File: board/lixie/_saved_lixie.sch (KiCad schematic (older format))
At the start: 41 parts, among them P1 USB_OTG, P2 CONN_01X04, SW1 SW_Push, U1 IS31FL3738, U2 MIC550x, U3 MAX40200, U4 STM32L073xZ

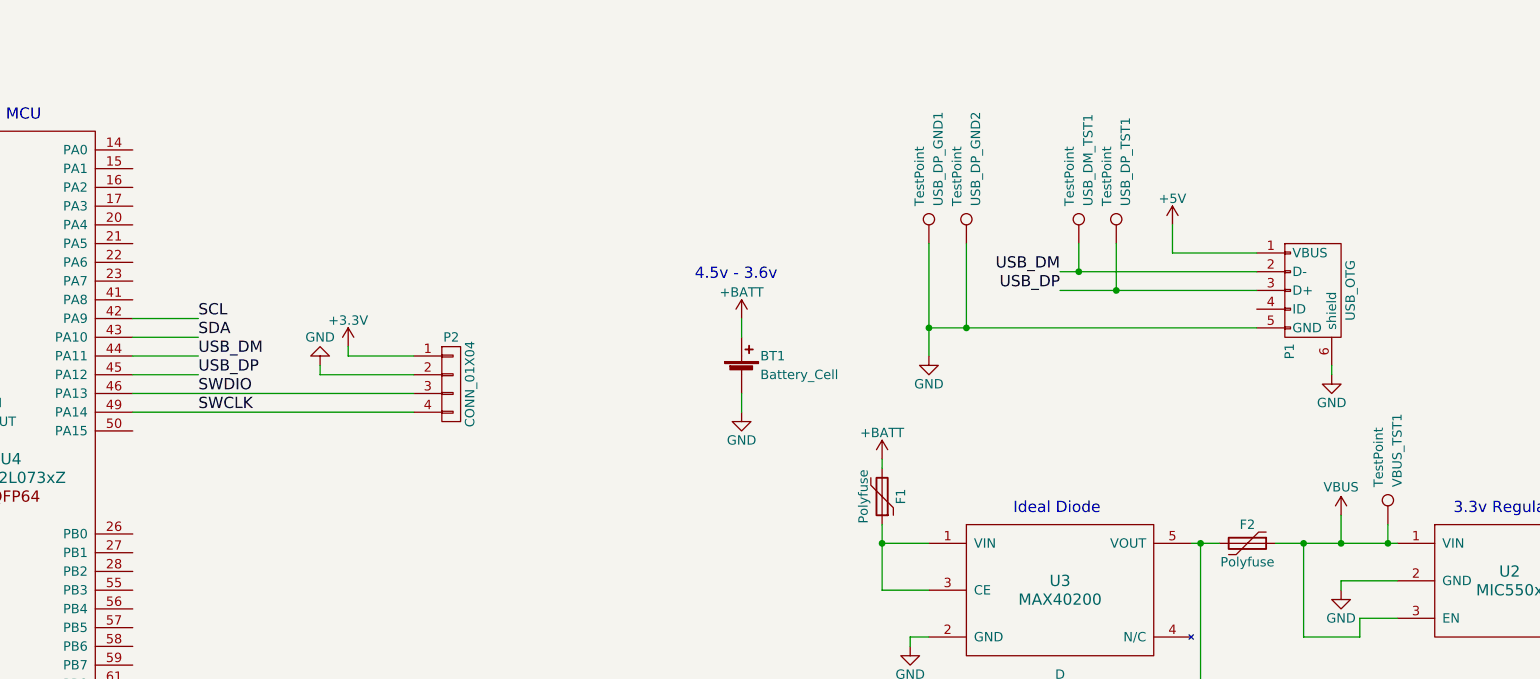
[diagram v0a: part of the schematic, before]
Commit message: apparently I routed EVERY FUCKING LED WRONG so now I gotta fix it
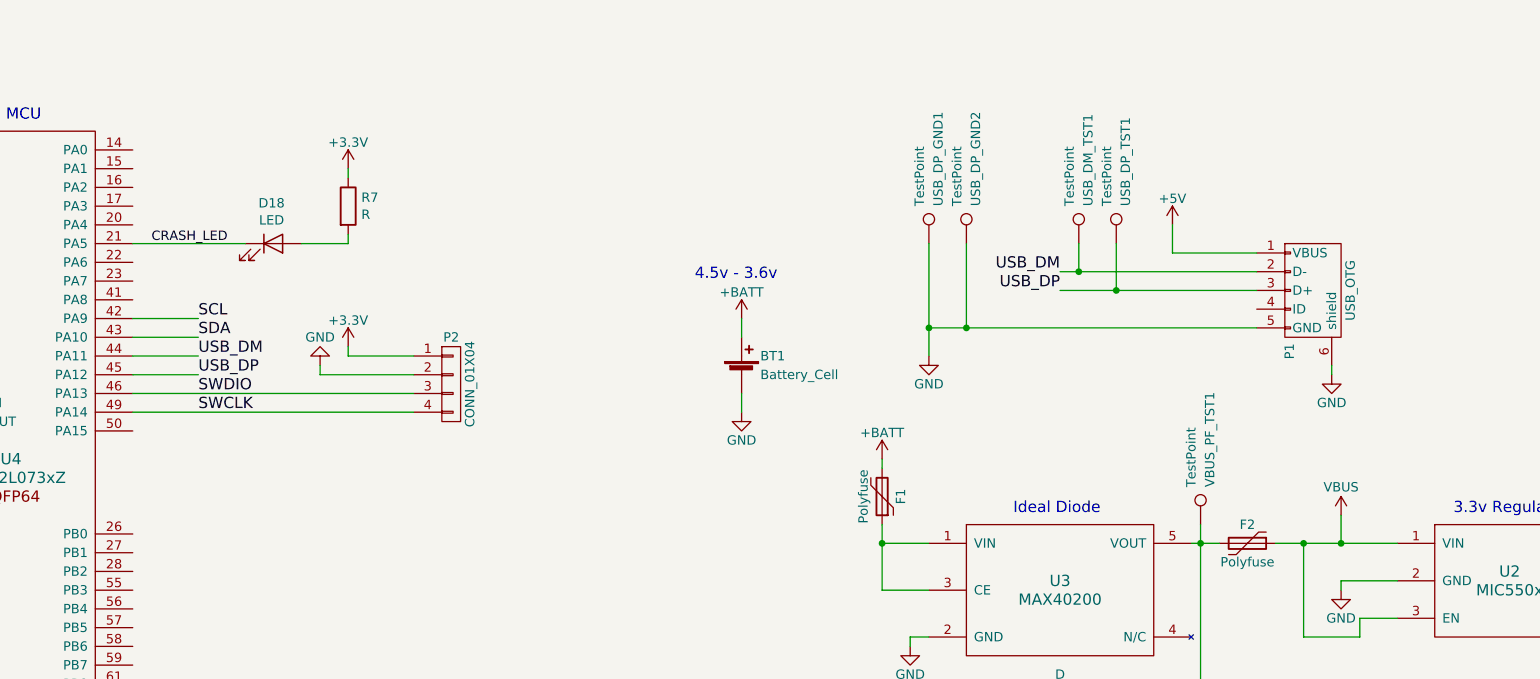
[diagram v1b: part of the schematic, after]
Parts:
- added D18: LED, LED_SMD:LED_0805_2012Metric_Pad1.15x1.40mm_HandSolder, symbol Device:LED
- added R7: R, Resistor_SMD:R_0805_2012Metric_Pad1.15x1.40mm_HandSolder, symbol Device:R
- D17: footprint Diodes_SMD:SOD-123 -> Diode_SMD:D_SOD-123
- F1, F2, F3: footprint Resistors_SMD:R_1206_HandSoldering -> Fuse:Fuse_1210_3225Metric_Pad1.42x2.65mm_HandSolder
- R1, R2, R3, R4, R5, R6: footprint Resistors_SMD:R_0805_HandSoldering -> Resistor_SMD:R_0805_2012Metric_Pad1.15x1.40mm_HandSolder
- renumbered VBUS_TST1 to VBUS_PF_TST1
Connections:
- net +3V3: now also R7.1
- net VBUS: no longer VBUS_PF_TST1.1
- net CRASH_LED: now reaches U4.21 (PA5)
- net CRASH_LED: now also D18.1 (K)
- net at D17.1 (K), F2.2, U3.5 (VOUT): now also VBUS_PF_TST1.1
- new net: D18.2 (A), R7.2
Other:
- moved on the sheet: VBUS_PF_TST1
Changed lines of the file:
@@
 F 0 "R3" V 4030 5550 50  0000 C CNN
 F 1 "100k" V 3950 5550 50  0000 C CNN
-F 2 "Resistors_SMD:R_0805_HandSoldering" V 3880 5550 50  0001 C CNN
+F 2 "Resistor_SMD:R_0805_2012Metric_Pad1.15x1.40mm_HandSolder" V 3880 5550 50  0001 C CNN
 F 3 "" H 3950 5550 50  0000 C CNN
 	1    3950 5550
@@
 F 0 "R2" V 3880 4950 50  0000 C CNN
 F 1 "100k" V 3800 4950 50  0000 C CNN
-F 2 "Resistors_SMD:R_0805_HandSoldering" V 3730 4950 50  0001 C CNN
+F 2 "Resistor_SMD:R_0805_2012Metric_Pad1.15x1.40mm_HandSolder" V 3730 4950 50  0001 C CNN
 F 3 "" H 3800 4950 50  0000 C CNN
 	1    3800 4950
@@
 F 0 "R1" V 3680 4950 50  0000 C CNN
 F 1 "100k" V 3600 4950 50  0000 C CNN
-F 2 "Resistors_SMD:R_0805_HandSoldering" V 3530 4950 50  0001 C CNN
+F 2 "Resistor_SMD:R_0805_2012Metric_Pad1.15x1.40mm_HandSolder" V 3530 4950 50  0001 C CNN
 F 3 "" H 3600 4950 50  0000 C CNN
 	1    3600 4950
@@
 F 0 "R4" V 3480 10200 50  0000 C CNN
 F 1 "10k" V 3400 10200 50  0000 C CNN
-F 2 "Resistors_SMD:R_0805_HandSoldering" V 3330 10200 50  0001 C CNN
+F 2 "Resistor_SMD:R_0805_2012Metric_Pad1.15x1.40mm_HandSolder" V 3330 10200 50  0001 C CNN
 F 3 "" H 3400 10200 50  0000 C CNN
 	1    3400 10200
@@
 F 0 "D17" H 10750 11350 50  0000 C CNN
 F 1 "D" H 10750 11150 50  0000 C CNN
-F 2 "Diodes_SMD:SOD-123" H 10750 11250 50  0001 C CNN
+F 2 "Diode_SMD:D_SOD-123" H 10750 11250 50  0001 C CNN
 F 3 "" H 10750 11250 50  0000 C CNN
 	1    10750 11250
@@
 F 0 "R6" V 4180 4100 50  0000 C CNN
 F 1 "4.7k" V 4100 4100 50  0000 C CNN
-F 2 "Resistors_SMD:R_0805_HandSoldering" V 4030 4100 50  0001 C CNN
+F 2 "Resistor_SMD:R_0805_2012Metric_Pad1.15x1.40mm_HandSolder" V 4030 4100 50  0001 C CNN
 F 3 "" H 4100 4100 50  0000 C CNN
 	1    4100 4100
@@
 F 0 "R5" V 3980 4100 50  0000 C CNN
 F 1 "4.7k" V 3900 4100 50  0000 C CNN
-F 2 "Resistors_SMD:R_0805_HandSoldering" V 3830 4100 50  0001 C CNN
+F 2 "Resistor_SMD:R_0805_2012Metric_Pad1.15x1.40mm_HandSolder" V 3830 4100 50  0001 C CNN
 F 3 "" H 3900 4100 50  0000 C CNN
 	1    3900 4100
@@
 F 0 "F2" V 11650 10450 50  0000 C CNN
 F 1 "Polyfuse" V 11850 10450 50  0000 C CNN
-F 2 "Resistors_SMD:R_1206_HandSoldering" H 11800 10250 50  0001 L CNN
+F 2 "Fuse:Fuse_1210_3225Metric_Pad1.42x2.65mm_HandSolder" H 11800 10250 50  0001 L CNN
 F 3 "" H 11750 10450 50  0001 C CNN
 	1    11750 10450
@@
 F 0 "F3" V 9700 11600 50  0000 C CNN
 F 1 "Polyfuse" V 9900 11600 50  0000 C CNN
-F 2 "Resistors_SMD:R_1206_HandSoldering" H 9850 11400 50  0001 L CNN
+F 2 "Fuse:Fuse_1210_3225Metric_Pad1.42x2.65mm_HandSolder" H 9850 11400 50  0001 L CNN
 F 3 "" H 9800 11600 50  0001 C CNN
 	1    9800 11600
@@
 F 0 "F1" V 9700 10200 50  0000 C CNN
 F 1 "Polyfuse" V 9900 10200 50  0000 C CNN
-F 2 "Resistors_SMD:R_1206_HandSoldering" H 9850 10000 50  0001 L CNN
+F 2 "Fuse:Fuse_1210_3225Metric_Pad1.42x2.65mm_HandSolder" H 9850 10000 50  0001 L CNN
 F 3 "" H 9800 10200 50  0001 C CNN
 	1    9800 10200
@@
 	11050 9100 11800 9100
 $Comp
-L Connector:TestPoint VBUS_TST1
+L Connector:TestPoint VBUS_PF_TST1
 U 1 1 5E499D81
-P 12500 10350
-F 0 "VBUS_TST1" V 12550 10550 50  0000 L CNN
-F 1 "TestPoint" V 12450 10550 50  0000 L CNN
-F 2 "Connector_PinHeader_2.54mm:PinHeader_1x01_P2.54mm_Vertical" H 12700 10350 50  0001 C CNN
-F 3 "~" H 12700 10350 50  0001 C CNN
-	1    12500 10350
-	1    0    0    -1
-$EndComp
-Wire Wire Line
-	12500 10350 12500 10450
-Wire Wire Line
-	12250 10450 12500 10450
-Connection ~ 12500 10450
-Wire Wire Line
-	12500 10450 12550 10450
+P 11500 10350
+F 0 "VBUS_PF_TST1" V 11550 10550 50  0000 L CNN
+F 1 "TestPoint" V 11450 10550 50  0000 L CNN
+F 2 "Connector_PinHeader_2.54mm:PinHeader_1x01_P2.54mm_Vertical" H 11700 10350 50  0001 C CNN
+F 3 "~" H 11700 10350 50  0001 C CNN
+	1    11500 10350
+	1    0    0    -1
+$EndComp
 $Comp
 L Connector:TestPoint USB_DP_GND2
@@
 Wire Wire Line
 	11350 8900 11800 8900
+Text Label 5900 8850 0    50   ~ 0
+CRASH_LED
+$Comp
+L Device:LED D18
+U 1 1 5E4BD99C
+P 6550 8850
+F 0 "D18" H 6541 9066 50  0000 C CNN
+F 1 "LED" H 6541 8975 50  0000 C CNN
+F 2 "LED_SMD:LED_0805_2012Metric_Pad1.15x1.40mm_HandSolder" H 6550 8850 50  0001 C CNN
+F 3 "~" H 6550 8850 50  0001 C CNN
+	1    6550 8850
+	1    0    0    -1
+$EndComp
+Wire Wire Line
+	6700 8850 6950 8850
+$Comp
+L Device:R R7
+U 1 1 5E4E9293
+P 6950 8650
+F 0 "R7" H 7020 8696 50  0000 L CNN
+F 1 "R" H 7020 8605 50  0000 L CNN
+F 2 "Resistor_SMD:R_0805_2012Metric_Pad1.15x1.40mm_HandSolder" V 6880 8650 50  0001 C CNN
+F 3 "~" H 6950 8650 50  0001 C CNN
+	1    6950 8650
+	1    0    0    -1
+$EndComp
+$Comp
+L lixie-rescue:+3.3V #PWR0101
+U 1 1 5E4EA8C3
+P 6950 8450
+F 0 "#PWR0101" H 6950 8300 50  0001 C CNN
+F 1 "+3.3V" H 6950 8590 50  0000 C CNN
+F 2 "" H 6950 8450 50  0001 C CNN
+F 3 "" H 6950 8450 50  0001 C CNN
+	1    6950 8450
+	1    0    0    -1
+$EndComp
+Wire Wire Line
+	6950 8450 6950 8500
+Wire Wire Line
+	6950 8800 6950 8850
+Wire Wire Line
+	5800 8850 6400 8850
+Wire Wire Line
+	12250 10450 12550 10450
+Wire Wire Line
+	11500 10450 11500 10350
 $EndSCHEMATC
